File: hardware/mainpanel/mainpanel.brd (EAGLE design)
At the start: 80 x 80 mm, 26 parts, among them J1 CDH, J2 OW, J3 DBG, J4 SUN-UART, J5 ADCS, J6 ENV, J7 SUN, U1 DS18B20, U2 DS18B20, U3 DS18B20

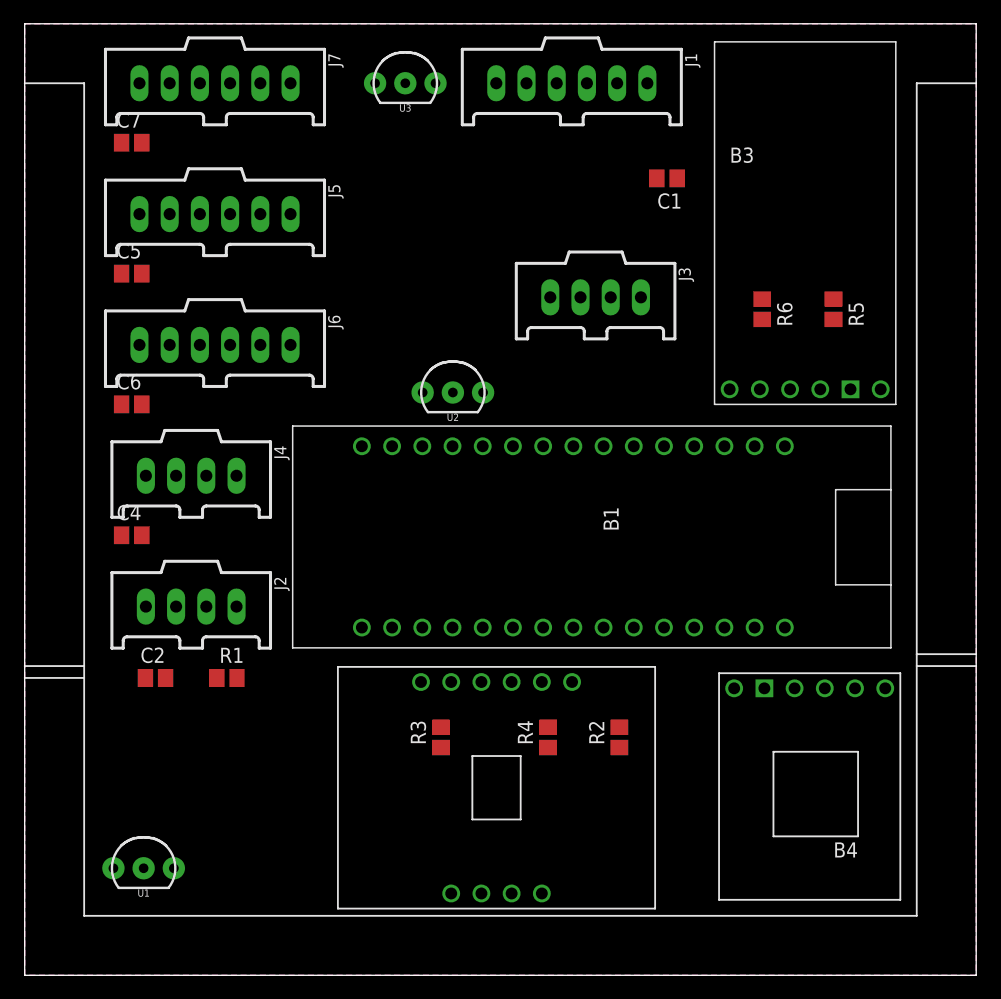
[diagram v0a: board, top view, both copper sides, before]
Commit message: Move caps/res to bot layer
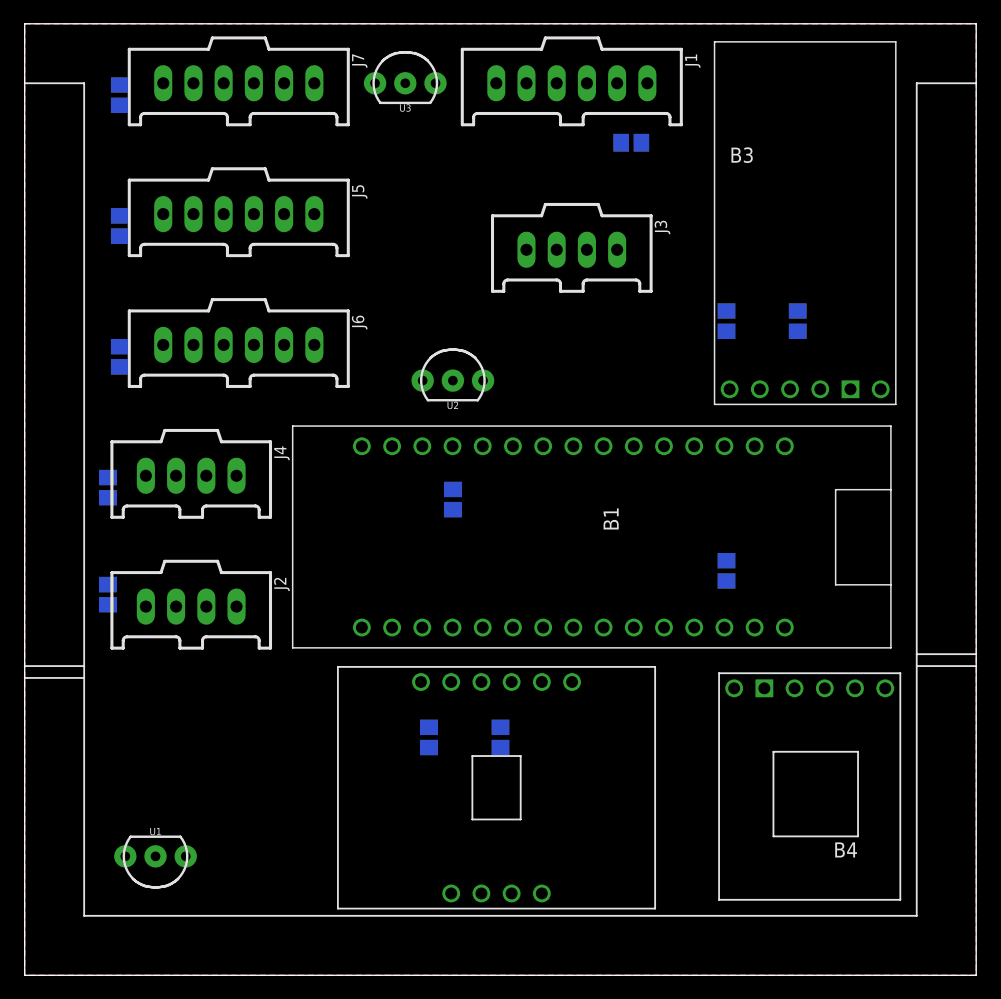
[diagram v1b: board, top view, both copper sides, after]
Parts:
- moved R1 24.2 mm to (36.0, 40.0), flipped to the bottom, turned to 270 degrees
- moved R2 16.6 mm to (59.0, 34.0), flipped to the bottom, turned to 270 degrees
- moved C2 8.06 mm to (7.00, 32.0), flipped to the bottom, turned to 90 degrees
- moved C4 4.47 mm to (7.00, 41.0), flipped to the bottom, turned to 90 degrees
- moved J3 4.47 mm to (46.0, 61.0)
- moved C1 4.24 mm to (51.0, 70.0), flipped to the bottom, turned to 0 degrees
- moved C5 4.12 mm to (8.00, 63.0), flipped to the bottom, turned to 90 degrees
- moved C6 4.12 mm to (8.00, 52.0), flipped to the bottom, turned to 90 degrees
- moved C7 4.12 mm to (8.00, 74.0), flipped to the bottom, turned to 90 degrees
- moved R4 4.00 mm to (40.0, 20.0), flipped to the bottom
- moved R5 3.16 mm to (65.0, 55.0), flipped to the bottom
- moved R6 3.16 mm to (59.0, 55.0), flipped to the bottom
- moved J5 2.00 mm to (18.0, 64.0)
- moved J6 2.00 mm to (18.0, 53.0)
- moved J7 2.00 mm to (18.0, 75.0)
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
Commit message: Set top plane to vcc
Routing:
- added copper zone on layer 1, net VCC
- removed copper zone on layer 1, net GND
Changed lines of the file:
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@@
 <contactref element="C6" pad="2"/>
 <contactref element="C7" pad="2"/>
-<wire x1="50.15" y1="70" x2="49.81" y2="75" width="0" layer="19" extent="16-16"/>
-<wire x1="34.54" y1="75" x2="49.81" y2="75" width="0" layer="19" extent="1-1"/>
-<wire x1="59" y1="55.85" x2="50.15" y2="70" width="0" layer="19" extent="16-16"/>
-<wire x1="65" y1="55.85" x2="59" y2="55.85" width="0" layer="19" extent="16-16"/>
-<wire x1="71.97" y1="49.27" x2="65" y2="55.85" width="0" layer="19" extent="16-16"/>
-<wire x1="59" y1="34.85" x2="71.97" y2="49.27" width="0" layer="19" extent="16-16"/>
-<wire x1="64.73" y1="24.128" x2="59" y2="34.85" width="0" layer="19" extent="16-16"/>
-<wire x1="46.02" y1="24.66" x2="59" y2="34.85" width="0" layer="19" extent="16-16"/>
-<wire x1="40" y1="19.15" x2="46.02" y2="24.66" width="0" layer="19" extent="16-16"/>
-<wire x1="34" y1="19.15" x2="40" y2="19.15" width="0" layer="19" extent="16-16"/>
-<wire x1="30.89" y1="29.24" x2="34" y2="19.15" width="0" layer="19" extent="16-16"/>
-<wire x1="36" y1="39.15" x2="30.89" y2="29.24" width="0" layer="19" extent="16-16"/>
-<wire x1="38.54" y1="50" x2="36" y2="39.15" width="0" layer="19" extent="16-16"/>
-<wire x1="12.73" y1="31" x2="30.89" y2="29.24" width="0" layer="19" extent="1-1"/>
-<wire x1="7" y1="32.85" x2="12.73" y2="31" width="0" layer="19" extent="16-16"/>
-<wire x1="7" y1="41.85" x2="7" y2="32.85" width="0" layer="19" extent="16-16"/>
-<wire x1="10.19" y1="42" x2="7" y2="41.85" width="0" layer="19" extent="16-16"/>
-<wire x1="8" y1="52.85" x2="7" y2="41.85" width="0" layer="19" extent="16-16"/>
-<wire x1="11.65" y1="53" x2="8" y2="52.85" width="0" layer="19" extent="16-16"/>
-<wire x1="11.65" y1="64" x2="11.65" y2="53" width="0" layer="19" extent="1-1"/>
-<wire x1="8" y1="63.85" x2="11.65" y2="64" width="0" layer="19" extent="16-16"/>
-<wire x1="11.65" y1="75" x2="11.65" y2="64" width="0" layer="19" extent="1-1"/>
-<wire x1="8" y1="74.85" x2="11.65" y2="75" width="0" layer="19" extent="16-16"/>
-<wire x1="8.46" y1="10" x2="12.73" y2="31" width="0" layer="19" extent="1-1"/>
-</signal>
-<signal name="GND">
-<contactref element="B1" pad="GND@2"/>
-<contactref element="B1" pad="GND@1"/>
-<contactref element="B2" pad="GND"/>
 <polygon width="0.1524" layer="1">
 <vertex x="0" y="80"/>
@@
 <vertex x="0" y="0"/>
 </polygon>
+<wire x1="59" y1="55.85" x2="65" y2="55.85" width="0" layer="19" extent="16-16"/>
+<wire x1="71.97" y1="49.27" x2="65" y2="55.85" width="0" layer="19" extent="16-16"/>
+<wire x1="7" y1="41.85" x2="10.19" y2="42" width="0" layer="19" extent="16-16"/>
+<wire x1="8" y1="74.85" x2="11.65" y2="75" width="0" layer="19" extent="16-16"/>
+<wire x1="8" y1="63.85" x2="11.65" y2="64" width="0" layer="19" extent="16-16"/>
+<wire x1="8" y1="52.85" x2="11.65" y2="53" width="0" layer="19" extent="16-16"/>
+<wire x1="50.15" y1="70" x2="49.81" y2="75" width="0" layer="19" extent="16-16"/>
+<wire x1="7" y1="32.85" x2="12.73" y2="31" width="0" layer="19" extent="16-16"/>
+<wire x1="40" y1="19.15" x2="46.02" y2="24.66" width="0" layer="19" extent="16-16"/>
+<wire x1="34" y1="19.15" x2="40" y2="19.15" width="0" layer="19" extent="16-16"/>
+<wire x1="36" y1="39.15" x2="30.89" y2="29.24" width="0" layer="19" extent="16-16"/>
+<wire x1="59" y1="34.85" x2="64.73" y2="24.128" width="0" layer="19" extent="16-16"/>
+</signal>
+<signal name="GND">
+<contactref element="B1" pad="GND@2"/>
+<contactref element="B1" pad="GND@1"/>
+<contactref element="B2" pad="GND"/>
 <contactref element="B3" pad="GND"/>
 <contactref element="B4" pad="GND"/>

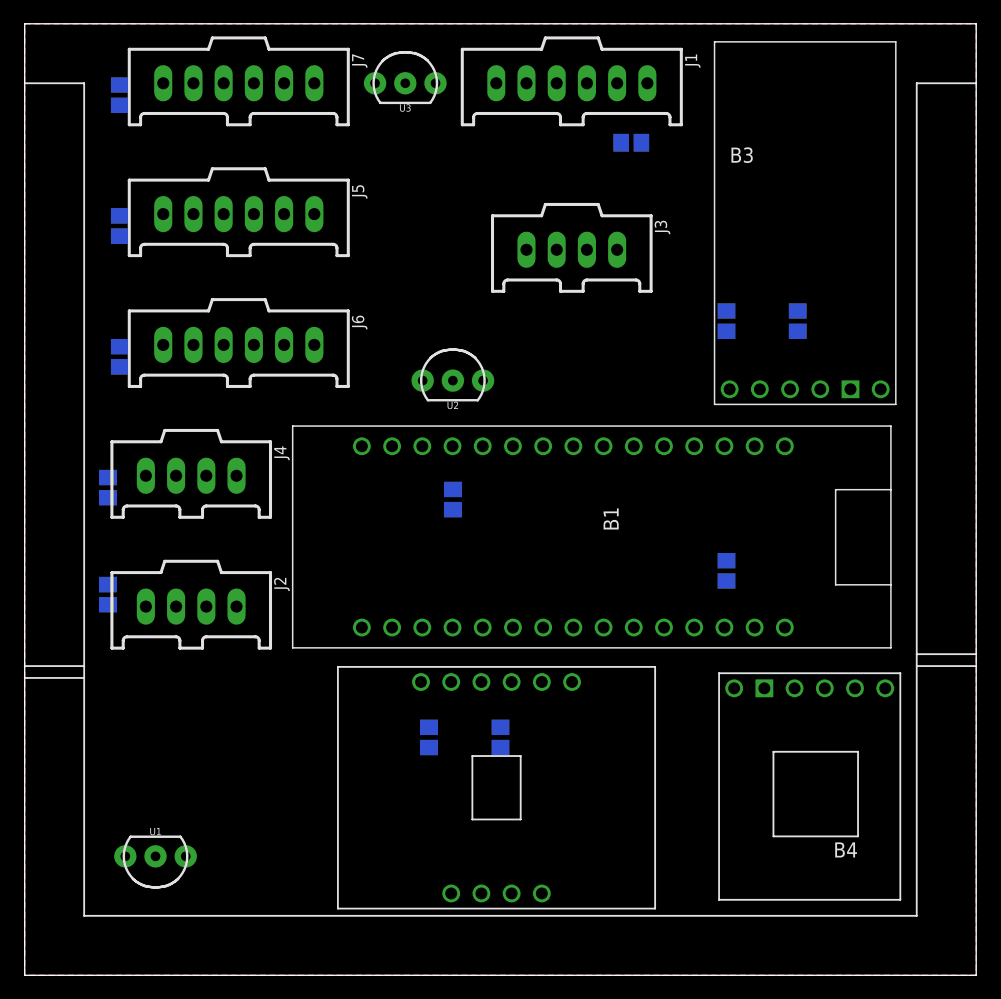
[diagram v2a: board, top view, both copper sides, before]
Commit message: Connect vcc pins to top plane
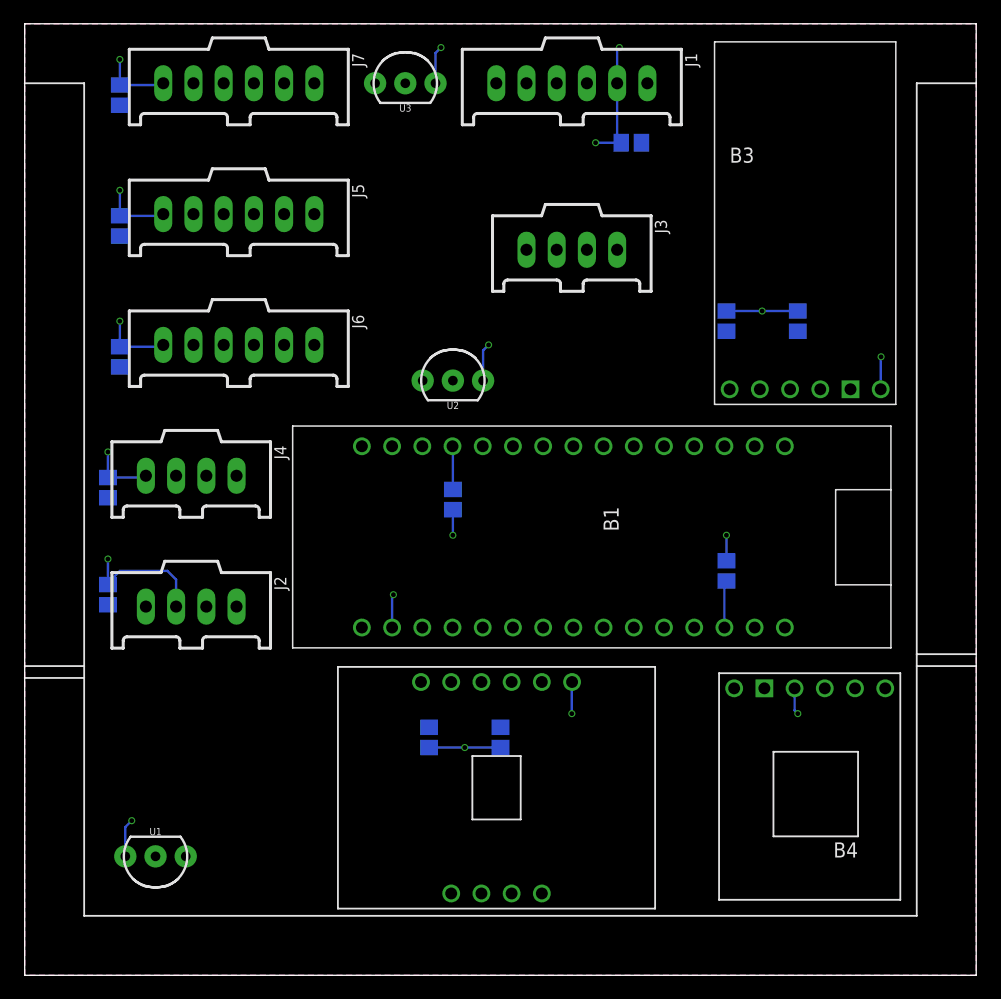
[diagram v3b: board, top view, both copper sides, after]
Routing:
- net VCC: track 0.00 -> 80.7 mm, vias 0 -> 18
- net N$1: track 0.00 -> 3.98 mm
- net TEMP-OW: track 0.00 -> 3.64 mm
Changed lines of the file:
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@@
 <vertex x="0" y="0"/>
 </polygon>
-<wire x1="59" y1="55.85" x2="65" y2="55.85" width="0" layer="19" extent="16-16"/>
-<wire x1="71.97" y1="49.27" x2="65" y2="55.85" width="0" layer="19" extent="16-16"/>
-<wire x1="7" y1="41.85" x2="10.19" y2="42" width="0" layer="19" extent="16-16"/>
-<wire x1="8" y1="74.85" x2="11.65" y2="75" width="0" layer="19" extent="16-16"/>
-<wire x1="8" y1="63.85" x2="11.65" y2="64" width="0" layer="19" extent="16-16"/>
-<wire x1="8" y1="52.85" x2="11.65" y2="53" width="0" layer="19" extent="16-16"/>
-<wire x1="50.15" y1="70" x2="49.81" y2="75" width="0" layer="19" extent="16-16"/>
-<wire x1="7" y1="32.85" x2="12.73" y2="31" width="0" layer="19" extent="16-16"/>
-<wire x1="40" y1="19.15" x2="46.02" y2="24.66" width="0" layer="19" extent="16-16"/>
-<wire x1="34" y1="19.15" x2="40" y2="19.15" width="0" layer="19" extent="16-16"/>
-<wire x1="36" y1="39.15" x2="30.89" y2="29.24" width="0" layer="19" extent="16-16"/>
-<wire x1="59" y1="34.85" x2="64.73" y2="24.128" width="0" layer="19" extent="16-16"/>
+<wire x1="49.81" y1="75" x2="49.81" y2="70.34" width="0.2" layer="16"/>
+<wire x1="49.81" y1="70.34" x2="50.15" y2="70" width="0.2" layer="16"/>
+<wire x1="50.15" y1="70" x2="48" y2="70" width="0.2" layer="16"/>
+<via x="48" y="70" extent="1-16" drill="0.4"/>
+<wire x1="49.81" y1="75" x2="49.81" y2="77.81" width="0.2" layer="16"/>
+<wire x1="49.81" y1="77.81" x2="50" y2="78" width="0.2" layer="16"/>
+<via x="50" y="78" extent="1-16" drill="0.4"/>
+<wire x1="34.54" y1="75" x2="34.54" y2="77.54" width="0.2" layer="16"/>
+<wire x1="34.54" y1="77.54" x2="35" y2="78" width="0.2" layer="16"/>
+<via x="35" y="78" extent="1-16" drill="0.4"/>
+<wire x1="11.65" y1="75" x2="11.5" y2="74.85" width="0.2" layer="16"/>
+<wire x1="11.5" y1="74.85" x2="8" y2="74.85" width="0.2" layer="16"/>
+<wire x1="11.65" y1="64" x2="11.5" y2="63.85" width="0.2" layer="16"/>
+<wire x1="11.5" y1="63.85" x2="8" y2="63.85" width="0.2" layer="16"/>
+<wire x1="11.65" y1="53" x2="11.5" y2="52.85" width="0.2" layer="16"/>
+<wire x1="11.5" y1="52.85" x2="8" y2="52.85" width="0.2" layer="16"/>
+<wire x1="10.19" y1="42" x2="10.04" y2="41.85" width="0.2" layer="16"/>
+<wire x1="10.04" y1="41.85" x2="7" y2="41.85" width="0.2" layer="16"/>
+<wire x1="12.73" y1="31" x2="12.73" y2="33.27" width="0.2" layer="16"/>
+<wire x1="12.73" y1="33.27" x2="12" y2="34" width="0.2" layer="16"/>
+<wire x1="12" y1="34" x2="8" y2="34" width="0.2" layer="16"/>
+<wire x1="8" y1="34" x2="7" y2="33" width="0.2" layer="16"/>
+<wire x1="7" y1="33" x2="7" y2="32.85" width="0.2" layer="16"/>
+<wire x1="8.46" y1="10" x2="8.46" y2="12.46" width="0.2" layer="16"/>
+<wire x1="8.46" y1="12.46" x2="9" y2="13" width="0.2" layer="16"/>
+<via x="9" y="13" extent="1-16" drill="0.4"/>
+<wire x1="7" y1="32.85" x2="7" y2="35" width="0.2" layer="16"/>
+<via x="7" y="35" extent="1-16" drill="0.4"/>
+<wire x1="7" y1="41.85" x2="7" y2="44" width="0.2" layer="16"/>
+<via x="7" y="44" extent="1-16" drill="0.4"/>
+<wire x1="8" y1="52.85" x2="8" y2="55" width="0.2" layer="16"/>
+<via x="8" y="55" extent="1-16" drill="0.4"/>
+<wire x1="8" y1="63.85" x2="8" y2="66" width="0.2" layer="16"/>
+<via x="8" y="66" extent="1-16" drill="0.4"/>
+<wire x1="8" y1="74.85" x2="8" y2="77" width="0.2" layer="16"/>
+<via x="8" y="77" extent="1-16" drill="0.4"/>
+<wire x1="38.54" y1="50" x2="38.54" y2="52.54" width="0.2" layer="16"/>
+<wire x1="38.54" y1="52.54" x2="39" y2="53" width="0.2" layer="16"/>
+<via x="39" y="53" extent="1-16" drill="0.4"/>
+<wire x1="59" y1="55.85" x2="62" y2="55.85" width="0.2" layer="16"/>
+<wire x1="62" y1="55.85" x2="65" y2="55.85" width="0.2" layer="16"/>
+<via x="62" y="55.85" extent="1-16" drill="0.4"/>
+<wire x1="71.97" y1="49.27" x2="71.97" y2="51.97" width="0.2" layer="16"/>
+<wire x1="71.97" y1="51.97" x2="72" y2="52" width="0.2" layer="16"/>
+<via x="72" y="52" extent="1-16" drill="0.4"/>
+<wire x1="30.89" y1="29.24" x2="30.89" y2="31.89" width="0.2" layer="16"/>
+<wire x1="30.89" y1="31.89" x2="31" y2="32" width="0.2" layer="16"/>
+<via x="31" y="32" extent="1-16" drill="0.4"/>
+<wire x1="34" y1="19.15" x2="37" y2="19.15" width="0.2" layer="16"/>
+<wire x1="37" y1="19.15" x2="40" y2="19.15" width="0.2" layer="16"/>
+<via x="37" y="19.15" extent="1-16" drill="0.4"/>
+<wire x1="46.02" y1="24.66" x2="46" y2="24.64" width="0.2" layer="16"/>
+<wire x1="46" y1="24.64" x2="46" y2="22" width="0.2" layer="16"/>
+<via x="46" y="22" extent="1-16" drill="0.4"/>
+<wire x1="64.73" y1="24.128" x2="64.73" y2="22.27" width="0.2" layer="16"/>
+<wire x1="64.73" y1="22.27" x2="65" y2="22" width="0.2" layer="16"/>
+<via x="65" y="22" extent="1-16" drill="0.4"/>
+<wire x1="59" y1="34.85" x2="59" y2="37" width="0.2" layer="16"/>
+<via x="59" y="37" extent="1-16" drill="0.4"/>
+<wire x1="36" y1="39.15" x2="36" y2="37" width="0.2" layer="16"/>
+<via x="36" y="37" extent="1-16" drill="0.4"/>
 </signal>
 <signal name="GND">
@@
 <contactref element="U3" pad="2"/>
 <contactref element="J2" pad="2"/>
+<wire x1="36" y1="40.85" x2="36" y2="44.45" width="0.2" layer="16"/>
+<wire x1="36" y1="44.45" x2="35.97" y2="44.48" width="0.2" layer="16"/>
 <wire x1="36" y1="50" x2="32" y2="75" width="0" layer="19" extent="1-1"/>
 <wire x1="35.97" y1="44.48" x2="36" y2="50" width="0" layer="19" extent="1-1"/>
-<wire x1="36" y1="40.85" x2="35.97" y2="44.48" width="0" layer="19" extent="16-16"/>
 <wire x1="15.27" y1="31" x2="36" y2="40.85" width="0" layer="19" extent="16-16"/>
 <wire x1="11" y1="10" x2="15.27" y2="31" width="0" layer="19" extent="1-1"/>
@@
 <contactref element="B1" pad="RST@2"/>
 <contactref element="R2" pad="2"/>
-<wire x1="58.83" y1="29.24" x2="59" y2="33.15" width="0" layer="19" extent="16-16"/>
+<wire x1="58.83" y1="29.24" x2="58.83" y2="32.98" width="0.2" layer="16"/>
+<wire x1="58.83" y1="32.98" x2="59" y2="33.15" width="0.2" layer="16"/>
 </signal>
 </signals>
